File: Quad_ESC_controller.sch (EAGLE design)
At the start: 28 parts, among them Y1 ECS-80-S-4X

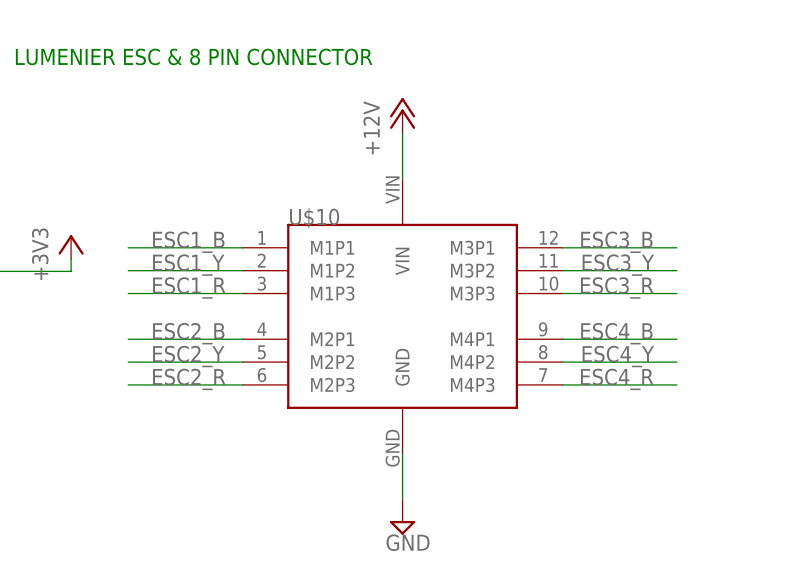
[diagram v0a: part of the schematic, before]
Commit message: remove lumenier and adjust size for controller
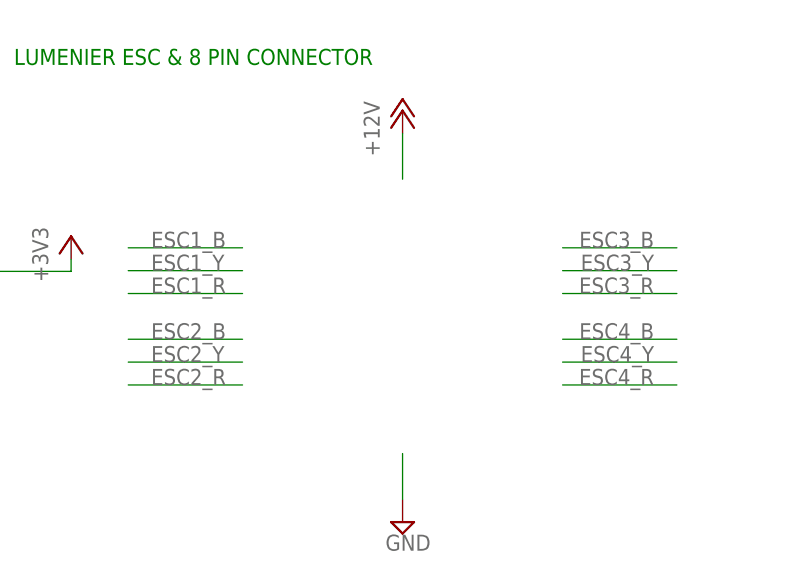
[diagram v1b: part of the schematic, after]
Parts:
- removed U$10: LUMENIER_QUAD, BLHeli_32 45A:LUMENIER_QUAD
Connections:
- net +12V: no longer U$10.VIN
- net ESC1_B: no longer U$10.M1P1
- net ESC1_R: no longer U$10.M1P3
- net ESC1_Y: no longer U$10.M1P2
- net ESC2_B: no longer U$10.M2P1
- net ESC2_R: no longer U$10.M2P3
- net ESC2_Y: no longer U$10.M2P2
- net ESC3_B: no longer U$10.M3P1
- net ESC3_R: no longer U$10.M3P3
- net ESC3_Y: no longer U$10.M3P2
- net ESC4_B: no longer U$10.M4P1
- net ESC4_R: no longer U$10.M4P3
- net ESC4_Y: no longer U$10.M4P2
- net GND: no longer U$10.GND
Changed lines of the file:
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@@
 <setting verticaltext="up"/>
 </settings>
-<grid distance="50" unitdist="mil" unit="mil" style="lines" multiple="1" display="no" altdistance="0.01" altunitdist="inch" altunit="inch"/>
+<grid distance="0.1" unitdist="inch" unit="inch" style="lines" multiple="1" display="no" altdistance="0.01" altunitdist="inch" altunit="inch"/>
 <layers>
 <layer number="1" name="Top" color="4" fill="1" visible="no" active="no"/>
@@
 <part name="R3" library="SparkFun-Resistors" library_urn="urn:adsk.eagle:library:532" deviceset="1KOHM" device="-0603-1/10W-1%" package3d_urn="urn:adsk.eagle:package:39650/1" value="1k"/>
 <part name="GND15" library="supply2" library_urn="urn:adsk.eagle:library:372" deviceset="GND" device=""/>
-<part name="U$10" library="BLHeli_32 45A" deviceset="LUMENIER_QUAD" device="" package3d_urn="urn:adsk.eagle:package:24294694/3"/>
 <part name="SUPPLY5" library="supply2" library_urn="urn:adsk.eagle:library:372" deviceset="GND" device=""/>
 <part name="P+5" library="supply1" library_urn="urn:adsk.eagle:library:371" deviceset="+12V" device=""/>
@@
 <attribute name="VALUE" x="501.015" y="52.705" size="1.778" layer="96"/>
 </instance>
-<instance part="U$10" gate="G$1" x="127" y="38.1" smashed="yes">
-<attribute name="NAME" x="114.3" y="48.26" size="1.778" layer="95"/>
-</instance>
 <instance part="SUPPLY5" gate="GND" x="127" y="15.24" smashed="yes">
 <attribute name="VALUE" x="125.095" y="12.065" size="1.778" layer="96"/>
@@
 </segment>
 <segment>
-<pinref part="U$10" gate="G$1" pin="GND"/>
 <wire x1="127" y1="22.86" x2="127" y2="17.78" width="0.1524" layer="91"/>
 <pinref part="SUPPLY5" gate="GND" pin="GND"/>
@@
 <net name="+12V" class="0">
 <segment>
-<pinref part="U$10" gate="G$1" pin="VIN"/>
 <wire x1="127" y1="53.34" x2="127" y2="58.42" width="0.1524" layer="91"/>
 <pinref part="P+5" gate="1" pin="+12V"/>
@@
 </segment>
 <segment>
-<pinref part="U$10" gate="G$1" pin="M4P1"/>
 <wire x1="144.78" y1="35.56" x2="157.48" y2="35.56" width="0.1524" layer="91"/>
 <label x="154.94" y="35.56" size="1.778" layer="95" align="bottom-right"/>
@@
 </segment>
 <segment>
-<pinref part="U$10" gate="G$1" pin="M4P2"/>
 <wire x1="144.78" y1="33.02" x2="157.48" y2="33.02" width="0.1524" layer="91"/>
 <label x="154.94" y="33.02" size="1.778" layer="95" align="bottom-right"/>
@@
 </segment>
 <segment>
-<pinref part="U$10" gate="G$1" pin="M4P3"/>
 <wire x1="144.78" y1="30.48" x2="157.48" y2="30.48" width="0.1524" layer="91"/>
 <label x="154.94" y="30.48" size="1.778" layer="95" align="bottom-right"/>
@@
 </segment>
 <segment>
-<pinref part="U$10" gate="G$1" pin="M3P1"/>
 <wire x1="144.78" y1="45.72" x2="157.48" y2="45.72" width="0.1524" layer="91"/>
 <label x="154.94" y="45.72" size="1.778" layer="95" align="bottom-right"/>
@@
 </segment>
 <segment>
-<pinref part="U$10" gate="G$1" pin="M3P2"/>
 <wire x1="144.78" y1="43.18" x2="157.48" y2="43.18" width="0.1524" layer="91"/>
 <label x="154.94" y="43.18" size="1.778" layer="95" align="bottom-right"/>
@@
 </segment>
 <segment>
-<pinref part="U$10" gate="G$1" pin="M3P3"/>
 <wire x1="144.78" y1="40.64" x2="157.48" y2="40.64" width="0.1524" layer="91"/>
 <label x="154.94" y="40.64" size="1.778" layer="95" align="bottom-right"/>
@@
 </segment>
 <segment>
-<pinref part="U$10" gate="G$1" pin="M2P1"/>
 <wire x1="109.22" y1="35.56" x2="96.52" y2="35.56" width="0.1524" layer="91"/>
 <label x="99.06" y="35.56" size="1.778" layer="95"/>
@@
 </segment>
 <segment>
-<pinref part="U$10" gate="G$1" pin="M2P2"/>
 <wire x1="109.22" y1="33.02" x2="96.52" y2="33.02" width="0.1524" layer="91"/>
 <label x="99.06" y="33.02" size="1.778" layer="95"/>
@@
 </segment>
 <segment>
-<pinref part="U$10" gate="G$1" pin="M2P3"/>
 <wire x1="109.22" y1="30.48" x2="96.52" y2="30.48" width="0.1524" layer="91"/>
 <label x="99.06" y="30.48" size="1.778" layer="95"/>
@@
 </segment>
 <segment>
-<pinref part="U$10" gate="G$1" pin="M1P1"/>
 <wire x1="109.22" y1="45.72" x2="96.52" y2="45.72" width="0.1524" layer="91"/>
 <label x="99.06" y="45.72" size="1.778" layer="95"/>
@@
 </segment>
 <segment>
-<pinref part="U$10" gate="G$1" pin="M1P2"/>
 <wire x1="109.22" y1="43.18" x2="96.52" y2="43.18" width="0.1524" layer="91"/>
 <label x="99.06" y="43.18" size="1.778" layer="95"/>
@@
 </segment>
 <segment>
-<pinref part="U$10" gate="G$1" pin="M1P3"/>
 <wire x1="109.22" y1="40.64" x2="96.52" y2="40.64" width="0.1524" layer="91"/>
 <label x="99.06" y="40.64" size="1.778" layer="95"/>

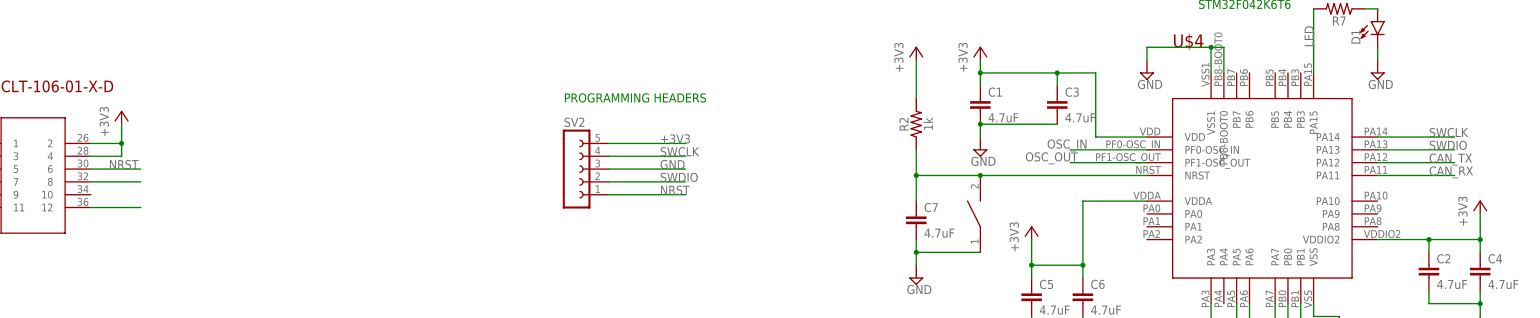
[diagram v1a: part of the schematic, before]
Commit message: Placement/Routing Update
the board and sch are out of sync and i have no idea how they got that way h e l p
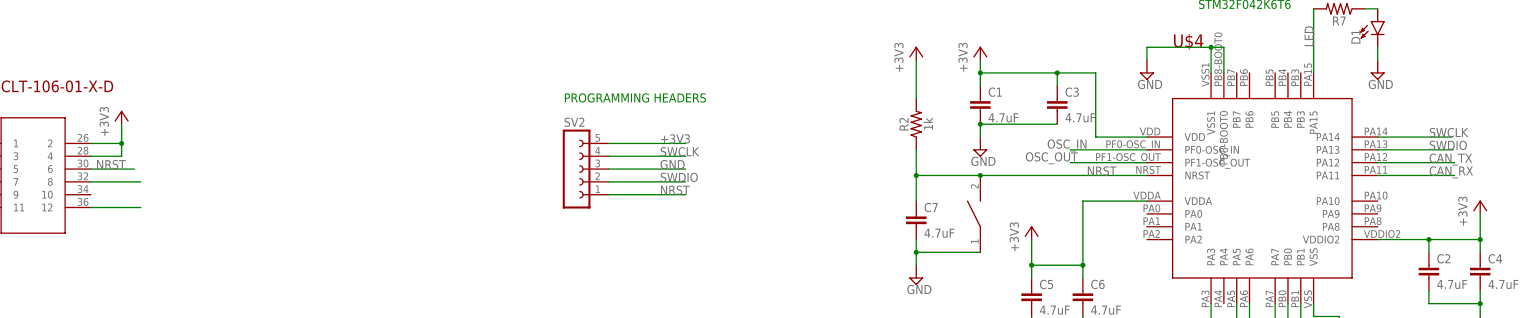
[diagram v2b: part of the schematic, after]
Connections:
- removed net NRST1: C7.1, R2.1, RESET.P$2, U$4.NRST
- net NRST: now also C7.1, R2.1, RESET.P$2, U$4.NRST
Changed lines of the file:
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@@
 <net name="SWDIO" class="0">
-<segment>
-<pinref part="U$4" gate="G$1" pin="PA13"/>
-<wire x1="492.76" y1="140.97" x2="508" y2="140.97" width="0.1524" layer="91"/>
-<label x="502.92" y="140.97" size="1.778" layer="95"/>
-</segment>
 <segment>
 <pinref part="SV2" gate="G$1" pin="2"/>
@@
 <label x="203.2" y="132.08" size="1.778" layer="95"/>
 </segment>
+<segment>
+<pinref part="U$4" gate="G$1" pin="PA13"/>
+<wire x1="492.76" y1="140.97" x2="507.746" y2="140.97" width="0.1524" layer="91"/>
+<label x="502.92" y="140.97" size="1.778" layer="95"/>
+</segment>
 </net>
 <net name="SWCLK" class="0">
-<segment>
-<pinref part="U$4" gate="G$1" pin="PA14"/>
-<wire x1="492.76" y1="143.51" x2="508" y2="143.51" width="0.1524" layer="91"/>
-<label x="502.92" y="143.51" size="1.778" layer="95"/>
-</segment>
 <segment>
 <pinref part="SV2" gate="G$1" pin="4"/>
@@
 <label x="203.2" y="129.54" size="1.778" layer="95"/>
 </segment>
-</net>
-<net name="NRST1" class="0">
 <segment>
-<pinref part="C7" gate="G$1" pin="1"/>
-<pinref part="R2" gate="G$1" pin="1"/>
-<wire x1="401.32" y1="140.97" x2="401.32" y2="135.89" width="0.1524" layer="91"/>
-<pinref part="RESET" gate="G$1" pin="P$2"/>
-<wire x1="401.32" y1="135.89" x2="401.32" y2="130.81" width="0.1524" layer="91"/>
-<wire x1="414.02" y1="135.89" x2="401.32" y2="135.89" width="0.1524" layer="91"/>
-<junction x="401.32" y="135.89"/>
-<pinref part="U$4" gate="G$1" pin="NRST"/>
-<wire x1="414.02" y1="135.89" x2="447.04" y2="135.89" width="0.1524" layer="91"/>
-<junction x="414.02" y="135.89"/>
+<pinref part="U$4" gate="G$1" pin="PA14"/>
+<wire x1="492.76" y1="143.51" x2="507.492" y2="143.51" width="0.1524" layer="91"/>
+<label x="502.92" y="143.51" size="1.778" layer="95"/>
 </segment>
 </net>
@@
 </segment>
 <segment>
+<pinref part="C7" gate="G$1" pin="1"/>
+<pinref part="R2" gate="G$1" pin="1"/>
+<wire x1="401.32" y1="140.97" x2="401.32" y2="135.89" width="0.1524" layer="91"/>
+<pinref part="RESET" gate="G$1" pin="P$2"/>
+<wire x1="401.32" y1="135.89" x2="401.32" y2="130.81" width="0.1524" layer="91"/>
+<wire x1="414.02" y1="135.89" x2="401.32" y2="135.89" width="0.1524" layer="91"/>
+<junction x="401.32" y="135.89"/>
+<pinref part="U$4" gate="G$1" pin="NRST"/>
+<wire x1="447.04" y1="135.89" x2="414.02" y2="135.89" width="0.1524" layer="91"/>
+<junction x="414.02" y="135.89"/>
+<label x="435.102" y="135.89" size="1.778" layer="95"/>
+</segment>
+<segment>
 <pinref part="U$3" gate="G$3" pin="6"/>
-<wire x1="237.744" y1="137.16" x2="247.65" y2="137.16" width="0.1524" layer="91"/>
-<label x="241.3" y="137.16" size="1.778" layer="95"/>
+<wire x1="237.744" y1="137.16" x2="246.38" y2="137.16" width="0.1524" layer="91"/>
+<label x="238.76" y="137.16" size="1.778" layer="95"/>
 </segment>
 </net>

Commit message: Placement/Routing Update
microcontroller movied to front, CAN signals length checked
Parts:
- removed U$1, U$5, U$6, U$7: 3PINCONNECTOR, BLHeli_32 45A:3PINCONNECTOR
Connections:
- removed net +12V: U$3G$1.1, U$3G$1.2, U$3G$1.3, U$3G$1.4, U$3G$1.5, U$3G$1.6, U$3G$1.7, U$3G$1.8, U$3G$2.1, U$3G$2.2, U$3G$2.3, U$3G$2.4, U$3G$2.5, U$3G$2.6, U$3G$2.7, U$3G$2.8
- removed net ESC1_B: U$1.A
- removed net ESC1_R: U$1.C
- removed net ESC1_Y: U$1.B
- removed net ESC2_B: U$5.A
- removed net ESC2_R: U$5.C
- removed net ESC2_Y: U$5.B
- removed net ESC3_B: U$6.A
- removed net ESC3_R: U$6.C
- removed net ESC3_Y: U$6.B
- removed net ESC4_B: U$7.A
- removed net ESC4_R: U$7.C
- removed net ESC4_Y: U$7.B
- net +3V3: now also U$3.1, U$3.2, U$3.3, U$3.4; no longer U$3G$3.1, U$3G$3.2, U$3G$3.3, U$3G$3.4
- net CAN_H: now also U$3.5; no longer U$3G$3.5
- net CAN_L: now also U$3.7; no longer U$3G$3.7
- net GND: no longer U$3G$1.10, U$3G$1.11, U$3G$1.12, U$3G$1.9, U$3G$2.10, U$3G$2.11, U$3G$2.12, U$3G$2.9
- net N$7: now also U$3.8; no longer U$3G$3.8
- net N$8: now also U$3.12; no longer U$3G$3.12
- net NRST: now also U$3.6; no longer U$3G$3.6
- net SWCLK: now also U$3.11; no longer U$3G$3.11
- net SWDIO: now also U$3.9; no longer U$3G$3.9
- net TIM3_CH1: now also U$4.PB1; no longer U$4.PA6
- net TIM3_CH2: now also U$4.PB0; no longer U$4.PA7
- net TIM3_CH3: now also U$4.PA7; no longer U$4.PB0
- net TIM3_CH4: now also U$4.PA6; no longer U$4.PB1
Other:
- note removed: "BACKPLANE CONNECTIONS"
- note removed: "LUMENIER ESC & 8 PIN CONNECTOR"
- note removed: "M1 3 Pin"
- note removed: "M2 3 Pin"
- note removed: "M3 3 Pin"
- note removed: "M4 3 Pin"
- note removed: "MOTOR 3PIN CONNECTORS"
- moved on the sheet: C1, C10, C2, C3, C4, C5, C6, C7, C8, C9, D1, R1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

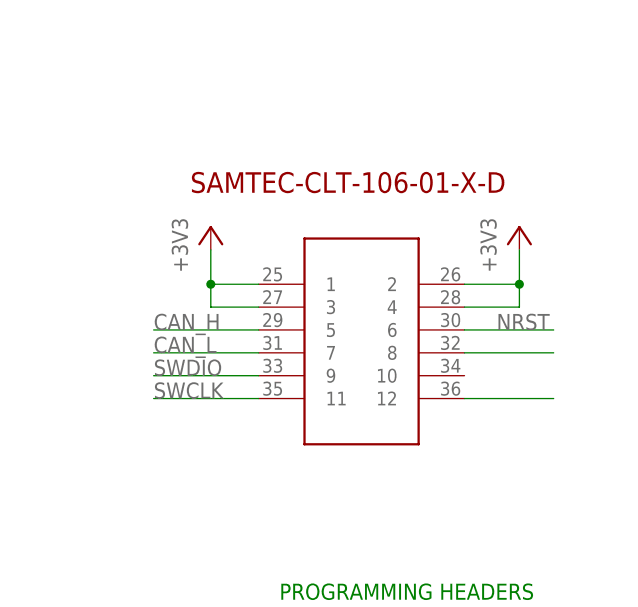
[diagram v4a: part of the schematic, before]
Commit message: Routing Update
rerouted new connector into board :)
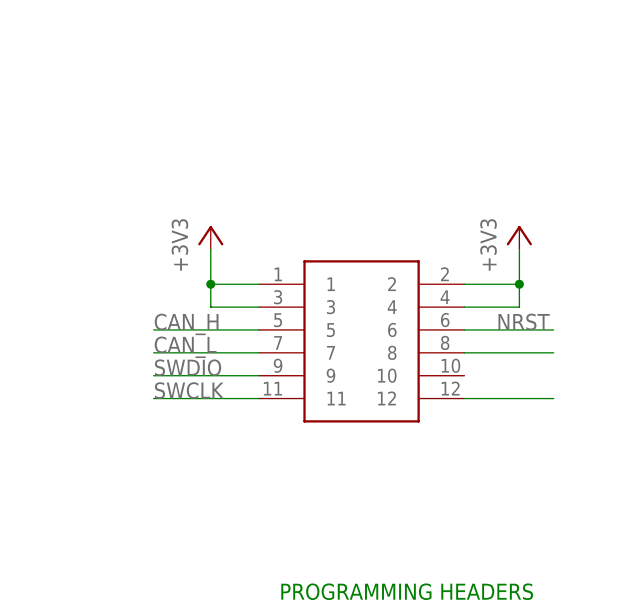
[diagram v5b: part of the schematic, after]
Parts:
- U$3: value BACKPLANE_CONNECTORS -> BACKPLANE_CONNECTORSBKP; device BLHeli_32 45A:BACKPLANE_CONNECTORS -> BLHeli_32 45A:BACKPLANE_CONNECTORSBKP
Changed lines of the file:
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@@
 <part name="SUPPLY7" library="SparkFun-PowerSymbols" library_urn="urn:adsk.eagle:library:530" deviceset="3.3V" device=""/>
 <part name="U$2" library="BLHeli_32 45A" deviceset="8PIN_CONNECTOR" device=""/>
-<part name="U$3" library="BLHeli_32 45A" deviceset="BACKPLANE_CONNECTORS" device=""/>
+<part name="U$3" library="BLHeli_32 45A" deviceset="BACKPLANE_CONNECTORS" device="BKP"/>
 <part name="+3V8" library="supply1" library_urn="urn:adsk.eagle:library:371" deviceset="+3V3" device=""/>
 <part name="+3V9" library="supply1" library_urn="urn:adsk.eagle:library:371" deviceset="+3V3" device=""/>
@@
 <instance part="SUPPLY7" gate="G$1" x="68.58" y="96.52" smashed="yes"/>
 <instance part="U$2" gate="G$1" x="149.86" y="38.1" smashed="yes" rot="R180"/>
-<instance part="U$3" gate="G$3" x="210.82" y="95.25" smashed="yes"/>
+<instance part="U$3" gate="G$1" x="210.82" y="95.25" smashed="yes"/>
 <instance part="+3V8" gate="G$1" x="194.31" y="107.95" smashed="yes">
 <attribute name="VALUE" x="191.77" y="102.87" size="1.778" layer="96" rot="R90"/>
@@
 </segment>
 <segment>
-<pinref part="U$3" gate="G$3" pin="1"/>
+<pinref part="U$3" gate="G$1" pin="1"/>
 <wire x1="199.644" y1="101.6" x2="194.31" y2="101.6" width="0.1524" layer="91"/>
 <wire x1="194.31" y1="101.6" x2="194.31" y2="105.41" width="0.1524" layer="91"/>
-<pinref part="U$3" gate="G$3" pin="3"/>
+<pinref part="U$3" gate="G$1" pin="3"/>
 <wire x1="199.644" y1="99.06" x2="194.31" y2="99.06" width="0.1524" layer="91"/>
 <wire x1="194.31" y1="99.06" x2="194.31" y2="101.6" width="0.1524" layer="91"/>
@@
 </segment>
 <segment>
-<pinref part="U$3" gate="G$3" pin="2"/>
+<pinref part="U$3" gate="G$1" pin="2"/>
 <wire x1="222.504" y1="101.6" x2="228.6" y2="101.6" width="0.1524" layer="91"/>
 <wire x1="228.6" y1="101.6" x2="228.6" y2="105.41" width="0.1524" layer="91"/>
-<pinref part="U$3" gate="G$3" pin="4"/>
+<pinref part="U$3" gate="G$1" pin="4"/>
 <wire x1="222.504" y1="99.06" x2="228.6" y2="99.06" width="0.1524" layer="91"/>
 <wire x1="228.6" y1="99.06" x2="228.6" y2="101.6" width="0.1524" layer="91"/>
@@
 </segment>
 <segment>
-<pinref part="U$3" gate="G$3" pin="5"/>
+<pinref part="U$3" gate="G$1" pin="5"/>
 <wire x1="199.644" y1="96.52" x2="187.96" y2="96.52" width="0.1524" layer="91"/>
 <label x="187.96" y="96.52" size="1.778" layer="95"/>
@@
 </segment>
 <segment>
-<pinref part="U$3" gate="G$3" pin="7"/>
+<pinref part="U$3" gate="G$1" pin="7"/>
 <wire x1="199.644" y1="93.98" x2="187.96" y2="93.98" width="0.1524" layer="91"/>
 <label x="187.96" y="93.98" size="1.778" layer="95"/>
@@
 </segment>
 <segment>
-<pinref part="U$3" gate="G$3" pin="9"/>
+<pinref part="U$3" gate="G$1" pin="9"/>
 <wire x1="199.644" y1="91.44" x2="187.96" y2="91.44" width="0.1524" layer="91"/>
 <label x="187.96" y="91.44" size="1.778" layer="95"/>
@@
 </segment>
 <segment>
-<pinref part="U$3" gate="G$3" pin="11"/>
+<pinref part="U$3" gate="G$1" pin="11"/>
 <wire x1="199.644" y1="88.9" x2="187.96" y2="88.9" width="0.1524" layer="91"/>
 <label x="187.96" y="88.9" size="1.778" layer="95"/>
@@
 </segment>
 <segment>
-<pinref part="U$3" gate="G$3" pin="6"/>
+<pinref part="U$3" gate="G$1" pin="6"/>
 <wire x1="222.504" y1="96.52" x2="232.41" y2="96.52" width="0.1524" layer="91"/>
 <label x="226.06" y="96.52" size="1.778" layer="95"/>
@@
 <net name="N$7" class="0">
 <segment>
-<pinref part="U$3" gate="G$3" pin="8"/>
+<pinref part="U$3" gate="G$1" pin="8"/>
 <wire x1="222.504" y1="93.98" x2="232.41" y2="93.98" width="0.1524" layer="91"/>
 </segment>
@@
 <net name="N$8" class="0">
 <segment>
-<pinref part="U$3" gate="G$3" pin="12"/>
+<pinref part="U$3" gate="G$1" pin="12"/>
 <wire x1="222.504" y1="88.9" x2="232.41" y2="88.9" width="0.1524" layer="91"/>
 </segment>
